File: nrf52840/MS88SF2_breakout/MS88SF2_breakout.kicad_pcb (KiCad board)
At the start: 2 copper layers, 25.6 x 36 mm, 3 parts, among them J1 Conn_01x14_Male, J2 Conn_01x14_Male, U1 MS88SF2

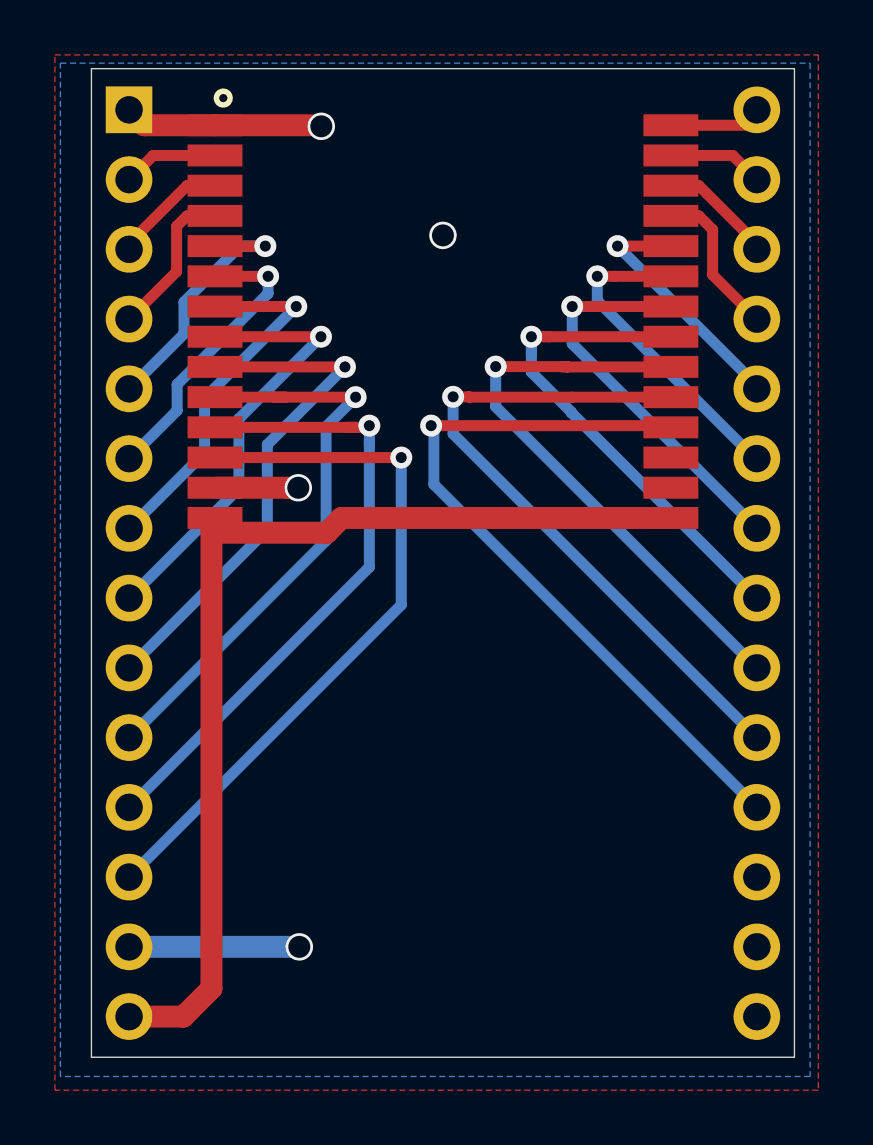
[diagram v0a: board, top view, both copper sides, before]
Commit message: nrf5: Improve grounding
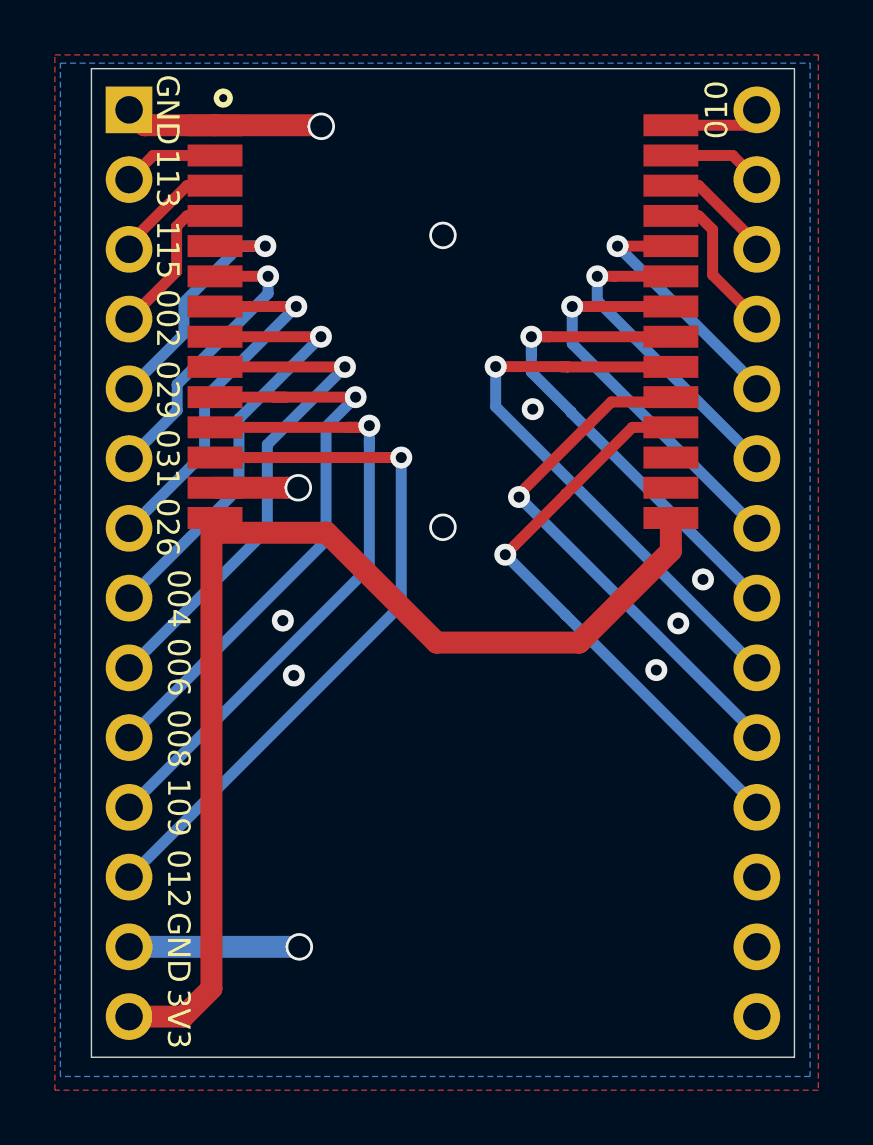
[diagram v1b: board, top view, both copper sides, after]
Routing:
- net P0.13: track 27.3 -> 20.9 mm
- net P0.15: track 24.9 -> 19.5 mm
- net +3V3: track 37.0 -> 41.0 mm
- net GND: vias 4 -> 11
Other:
- board text added: "002"
- board text added: "004"
- board text added: "006"
- board text added: "008"
- board text added: "010"
- board text added: "012"
- board text added: "026"
- board text added: "029"
- board text added: "031"
- board text added: "109"
- board text added: "113"
- board text added: "115"
- board text added: "3V3"
- board text added: "GND"

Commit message: nrf5: Add 10u cap
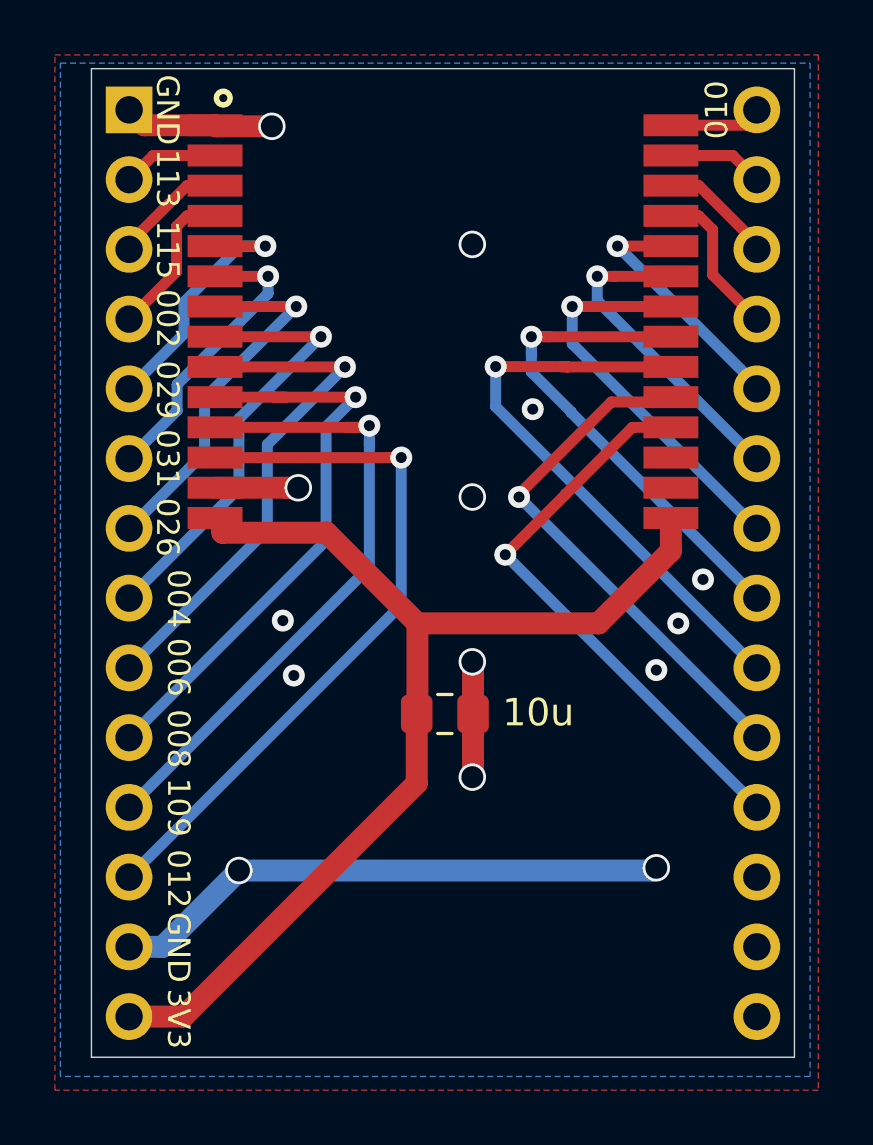
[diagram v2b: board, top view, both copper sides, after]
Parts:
- added C1: 10uF, Capacitor_SMD:C_0805_2012Metric_Pad1.15x1.40mm_HandSolder, F.Cu at (74.5, 82.0)
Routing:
- net GND: track 16.5 -> 33.1 mm, vias 11 -> 14
- net +3V3: track 41.0 -> 40.5 mm
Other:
- board text added: "10u"

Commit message: nrf5: Adjust silk screen
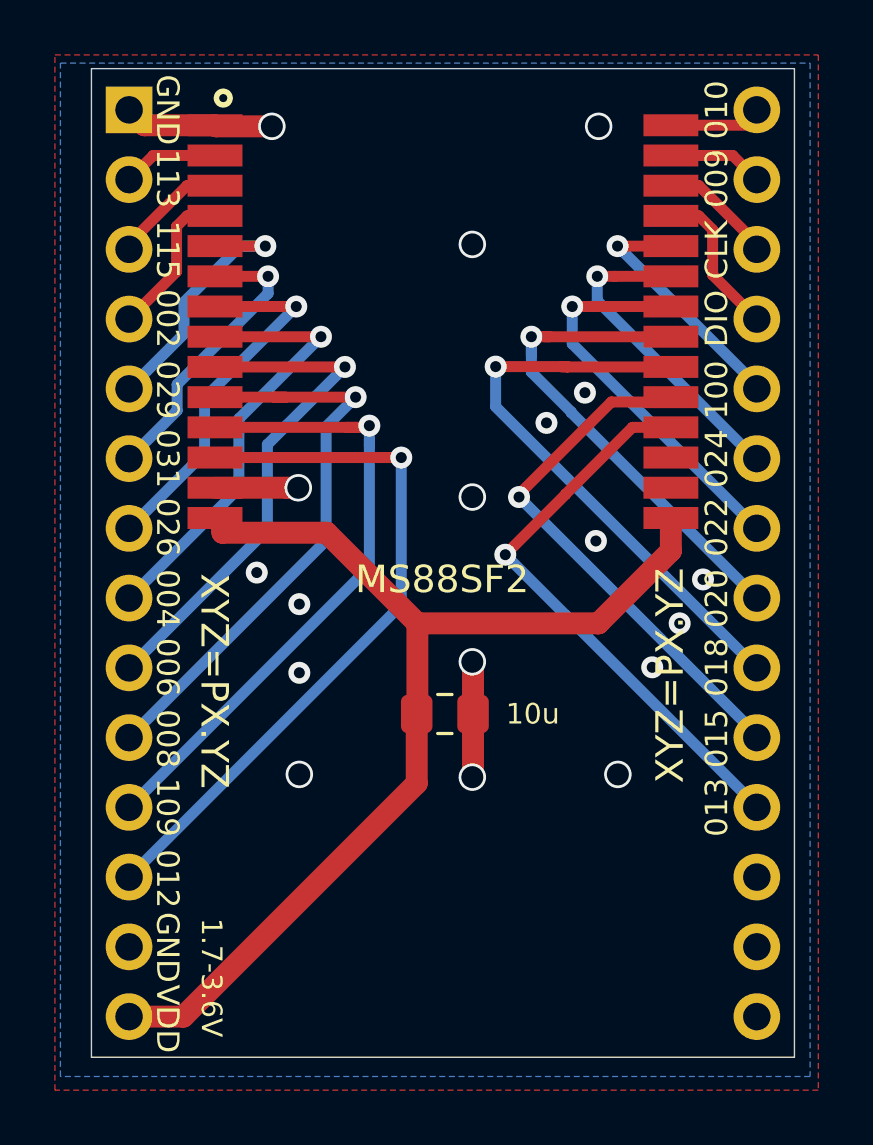
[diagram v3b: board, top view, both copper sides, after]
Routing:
- net GND: track 33.1 -> 12.7 mm, vias 14 -> 18
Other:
- board text added: "009"
- board text added: "013"
- board text added: "015"
- board text added: "018"
- board text added: "020"
- board text added: "022"
- board text added: "024"
- board text added: "1.7-3.6V"
- board text added: "100"
- board text added: "CLK"
- board text added: "DIO"
- board text added: "MS88SF2"
- board text added: "VDD"
- board text added: "XYZ=PX.YZ"
- board text added: "revA"
- board text removed: "3V3"
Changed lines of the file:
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@@
   (general
     (thickness 1.6)
-    (drawings 22)
+    (drawings 37)
     (tracks 162)
     (zones 0)
@@
     (47 F.CrtYd user)
     (48 B.Fab user)
-    (49 F.Fab user hide)
+    (49 F.Fab user)
   )
   (setup
-    (last_trace_width 0.8)
+    (last_trace_width 0.25)
     (user_trace_width 0.3)
     (user_trace_width 0.4)
@@
       (outputformat 1)
       (mirror false)
-      (drillshape 1)
+      (drillshape 0)
       (scaleselection 1)
-      (outputdirectory ""))
+      (outputdirectory "!gerbs/"))
   )
   (net 0 "")
@@
       (effects (font (size 0.5 0.5) (thickness 0.08)))
     )
-    (pad 1 smd roundrect (at -1.025 0) (size 1.15 1.4) (layers F.Cu F.Paste F.Mask) (roundrect_rratio 0.217391)
+    (pad 1 smd roundrect (at -1.025 0) (size 1.15 1.4) (layers F.Cu F.Paste F.Mask) (roundrect_rratio 0.2173904347826087)
       (net 1 +3V3))
-    (pad 2 smd roundrect (at 1.025 0) (size 1.15 1.4) (layers F.Cu F.Paste F.Mask) (roundrect_rratio 0.217391)
+    (pad 2 smd roundrect (at 1.025 0) (size 1.15 1.4) (layers F.Cu F.Paste F.Mask) (roundrect_rratio 0.2173904347826087)
       (net 2 GND))
     (model ${KISYS3DMOD}/Capacitor_SMD.3dshapes/C_0805_2012Metric.wrl
@@
     )
   )
-  (gr_text 10u (at 77.9 81.95) (layer F.SilkS)
+  (gr_text revA (at 83 93.5) (layer B.SilkS)
+    (effects (font (size 0.75 0.75) (thickness 0.15)) (justify mirror))
+  )
+  (gr_text 1.7-3.6V (at 66 91.6 -90) (layer F.SilkS)
+    (effects (font (size 0.75 0.75) (thickness 0.15)))
+  )
+  (gr_text XYZ=PX.YZ (at 82.7 80.6 90) (layer F.SilkS)
     (effects (font (size 1 1) (thickness 0.15)))
   )
+  (gr_text XYZ=PX.YZ (at 66.1 80.8 270) (layer F.SilkS)
+    (effects (font (size 1 1) (thickness 0.15)))
+  )
+  (gr_text MS88SF2 (at 74.4 77.1) (layer F.SilkS)
+    (effects (font (size 1 1) (thickness 0.15)))
+  )
+  (gr_text 013 (at 84.4 85.4 90) (layer F.SilkS)
+    (effects (font (size 0.82 0.82) (thickness 0.154)))
+  )
+  (gr_text 015 (at 84.4 82.9 90) (layer F.SilkS)
+    (effects (font (size 0.82 0.82) (thickness 0.154)))
+  )
+  (gr_text 018 (at 84.4 80.3 90) (layer F.SilkS)
+    (effects (font (size 0.82 0.82) (thickness 0.154)))
+  )
+  (gr_text 020 (at 84.4 77.8 90) (layer F.SilkS)
+    (effects (font (size 0.82 0.82) (thickness 0.154)))
+  )
+  (gr_text 022 (at 84.4 75.2 90) (layer F.SilkS)
+    (effects (font (size 0.82 0.82) (thickness 0.154)))
+  )
+  (gr_text 024 (at 84.4 72.7 90) (layer F.SilkS)
+    (effects (font (size 0.82 0.82) (thickness 0.154)))
+  )
+  (gr_text 100 (at 84.4 70.2 90) (layer F.SilkS)
+    (effects (font (size 0.82 0.82) (thickness 0.154)))
+  )
+  (gr_text DIO (at 84.4 67.6 90) (layer F.SilkS)
+    (effects (font (size 0.82 0.82) (thickness 0.154)))
+  )
+  (gr_text CLK (at 84.4 65.1 90) (layer F.SilkS)
+    (effects (font (size 0.82 0.82) (thickness 0.154)))
+  )
+  (gr_text 009 (at 84.4 62.5 90) (layer F.SilkS)
+    (effects (font (size 0.82 0.82) (thickness 0.154)))
+  )
+  (gr_text 10u (at 77.7 82) (layer F.SilkS)
+    (effects (font (size 0.75 0.75) (thickness 0.15)))
+  )
   (gr_text 010 (at 84.4 60 90) (layer F.SilkS)
     (effects (font (size 0.82 0.82) (thickness 0.154)))
   )
-  (gr_text 3V3 (at 64.8 93.1 -90) (layer F.SilkS)
-    (effects (font (size 0.82 0.82) (thickness 0.154)))
-  )
-  (gr_text GND (at 64.8 90.5 -90) (layer F.SilkS)
-    (effects (font (size 0.82 0.82) (thickness 0.154)))
-  )
-  (gr_text 012 (at 64.8 88 -90) (layer F.SilkS)
-    (effects (font (size 0.82 0.82) (thickness 0.154)))
-  )
-  (gr_text 109 (at 64.8 85.4 -90) (layer F.SilkS)
-    (effects (font (size 0.82 0.82) (thickness 0.154)))
-  )
-  (gr_text 008 (at 64.8 82.9 -90) (layer F.SilkS)
-    (effects (font (size 0.82 0.82) (thickness 0.154)))
-  )
-  (gr_text 006 (at 64.8 80.3 -90) (layer F.SilkS)
-    (effects (font (size 0.82 0.82) (thickness 0.154)))
-  )
-  (gr_text 004 (at 64.8 77.8 -90) (layer F.SilkS)
+  (gr_text VDD (at 64.4 93.1 -90) (layer F.SilkS)
+    (effects (font (size 0.82 0.82) (thickness 0.154)))
+  )
+  (gr_text GND (at 64.4 90.5 -90) (layer F.SilkS)
+    (effects (font (size 0.82 0.82) (thickness 0.154)))
+  )
+  (gr_text 012 (at 64.4 88 -90) (layer F.SilkS)
+    (effects (font (size 0.82 0.82) (thickness 0.154)))
+  )
+  (gr_text 109 (at 64.4 85.4 -90) (layer F.SilkS)
+    (effects (font (size 0.82 0.82) (thickness 0.154)))
+  )
+  (gr_text 008 (at 64.4 82.9 -90) (layer F.SilkS)
+    (effects (font (size 0.82 0.82) (thickness 0.154)))
+  )
+  (gr_text 006 (at 64.4 80.3 -90) (layer F.SilkS)
+    (effects (font (size 0.82 0.82) (thickness 0.154)))
+  )
+  (gr_text 004 (at 64.4 77.8 -90) (layer F.SilkS)
     (effects (font (size 0.82 0.82) (thickness 0.154)))
   )
@@
   (segment (start 69.162 73.762) (end 68.762 73.762) (width 0.8) (layer F.Cu) (net 2))
   (via (at 69.162 73.762) (size 1) (drill 0.8) (layers F.Cu B.Cu) (net 2))
-  (via (at 67 87.7) (size 1) (drill 0.8) (layers F.Cu B.Cu) (net 2))
+  (via (at 69.2 84.2) (size 1) (drill 0.8) (layers F.Cu B.Cu) (net 2))
   (via (at 75.5 64.9) (size 1) (drill 0.8) (layers F.Cu B.Cu) (net 2))
   (via (at 68.2 60.6) (size 1) (drill 0.8) (layers F.Cu B.Cu) (net 2))
@@
   (segment (start 66.13 60.562) (end 63.562 60.562) (width 0.8) (layer F.Cu) (net 2) (status 30))
   (via (at 75.5 74.1) (size 1) (drill 0.8) (layers F.Cu B.Cu) (net 2))
-  (via (at 82.2 80.4) (size 0.8) (drill 0.4) (layers F.Cu B.Cu) (net 2))
-  (via (at 83 78.7) (size 0.8) (drill 0.4) (layers F.Cu B.Cu) (net 2))
+  (via (at 82.05 80.3) (size 0.8) (drill 0.4) (layers F.Cu B.Cu) (net 2))
+  (via (at 83.05 78.7) (size 0.8) (drill 0.4) (layers F.Cu B.Cu) (net 2))
   (via (at 83.9 77.1) (size 0.8) (drill 0.4) (layers F.Cu B.Cu) (net 2))
-  (via (at 77.7 70.9) (size 0.8) (drill 0.4) (layers F.Cu B.Cu) (net 2))
-  (via (at 69 80.6) (size 0.8) (drill 0.4) (layers F.Cu B.Cu) (net 2))
-  (via (at 68.6 78.6) (size 0.8) (drill 0.4) (layers F.Cu B.Cu) (net 2))
-  (segment (start 64.22 90.48) (end 67 87.7) (width 0.8) (layer B.Cu) (net 2))
-  (segment (start 63 90.48) (end 64.22 90.48) (width 0.8) (layer B.Cu) (net 2))
-  (via (at 82.2 87.6) (size 1) (drill 0.8) (layers F.Cu B.Cu) (net 2))
-  (segment (start 82.1 87.7) (end 82.2 87.6) (width 0.8) (layer B.Cu) (net 2))
-  (segment (start 67 87.7) (end 82.1 87.7) (width 0.8) (layer B.Cu) (net 2))
+  (via (at 69.2 80.5) (size 0.8) (drill 0.4) (layers F.Cu B.Cu) (net 2))
+  (via (at 69.2 78) (size 0.8) (drill 0.4) (layers F.Cu B.Cu) (net 2))
+  (via (at 80.8 84.2) (size 1) (drill 0.8) (layers F.Cu B.Cu) (net 2))
   (via (at 75.5 80.1) (size 1) (drill 0.8) (layers F.Cu B.Cu) (net 2))
   (via (at 75.5 84.3) (size 1) (drill 0.8) (layers F.Cu B.Cu) (net 2))
@@
   (segment (start 66.168 60.6) (end 66.13 60.562) (width 0.8) (layer F.Cu) (net 2))
   (segment (start 68.2 60.6) (end 66.168 60.6) (width 0.8) (layer F.Cu) (net 2))
+  (via (at 67.65 76.85) (size 0.8) (drill 0.4) (layers F.Cu B.Cu) (net 2))
+  (via (at 79.6 70.3) (size 0.8) (drill 0.4) (layers F.Cu B.Cu) (net 2))
+  (via (at 78.2 71.4) (size 0.8) (drill 0.4) (layers F.Cu B.Cu) (net 2))
+  (via (at 80 75.7) (size 0.8) (drill 0.4) (layers F.Cu B.Cu) (net 2))
+  (via (at 80.1 60.6) (size 1) (drill 0.8) (layers F.Cu B.Cu) (net 2))
   (segment (start 82.73 60.562) (end 83.438 60.562) (width 0.4) (layer F.Cu) (net 3) (status 30))
   (segment (start 85.69801 60.562) (end 85.86 60.40001) (width 0.4) (layer F.Cu) (net 3) (status 30))
